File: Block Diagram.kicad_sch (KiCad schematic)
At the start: 0 parts

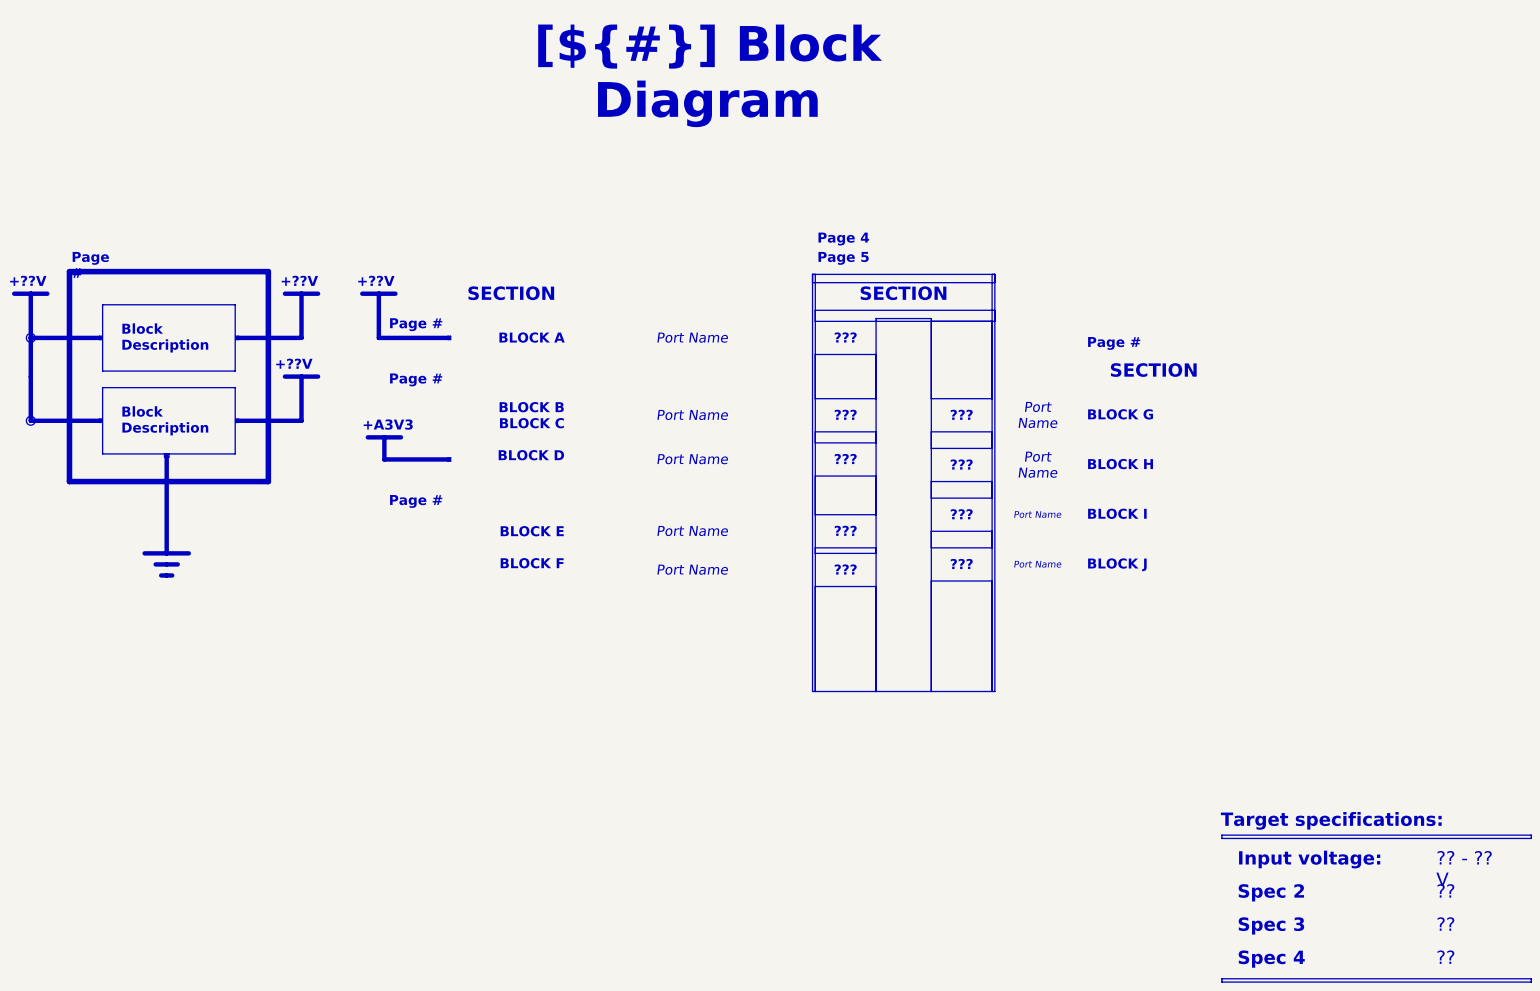
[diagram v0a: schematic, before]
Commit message: feat: Added some design notes, fixed some values in line with sim
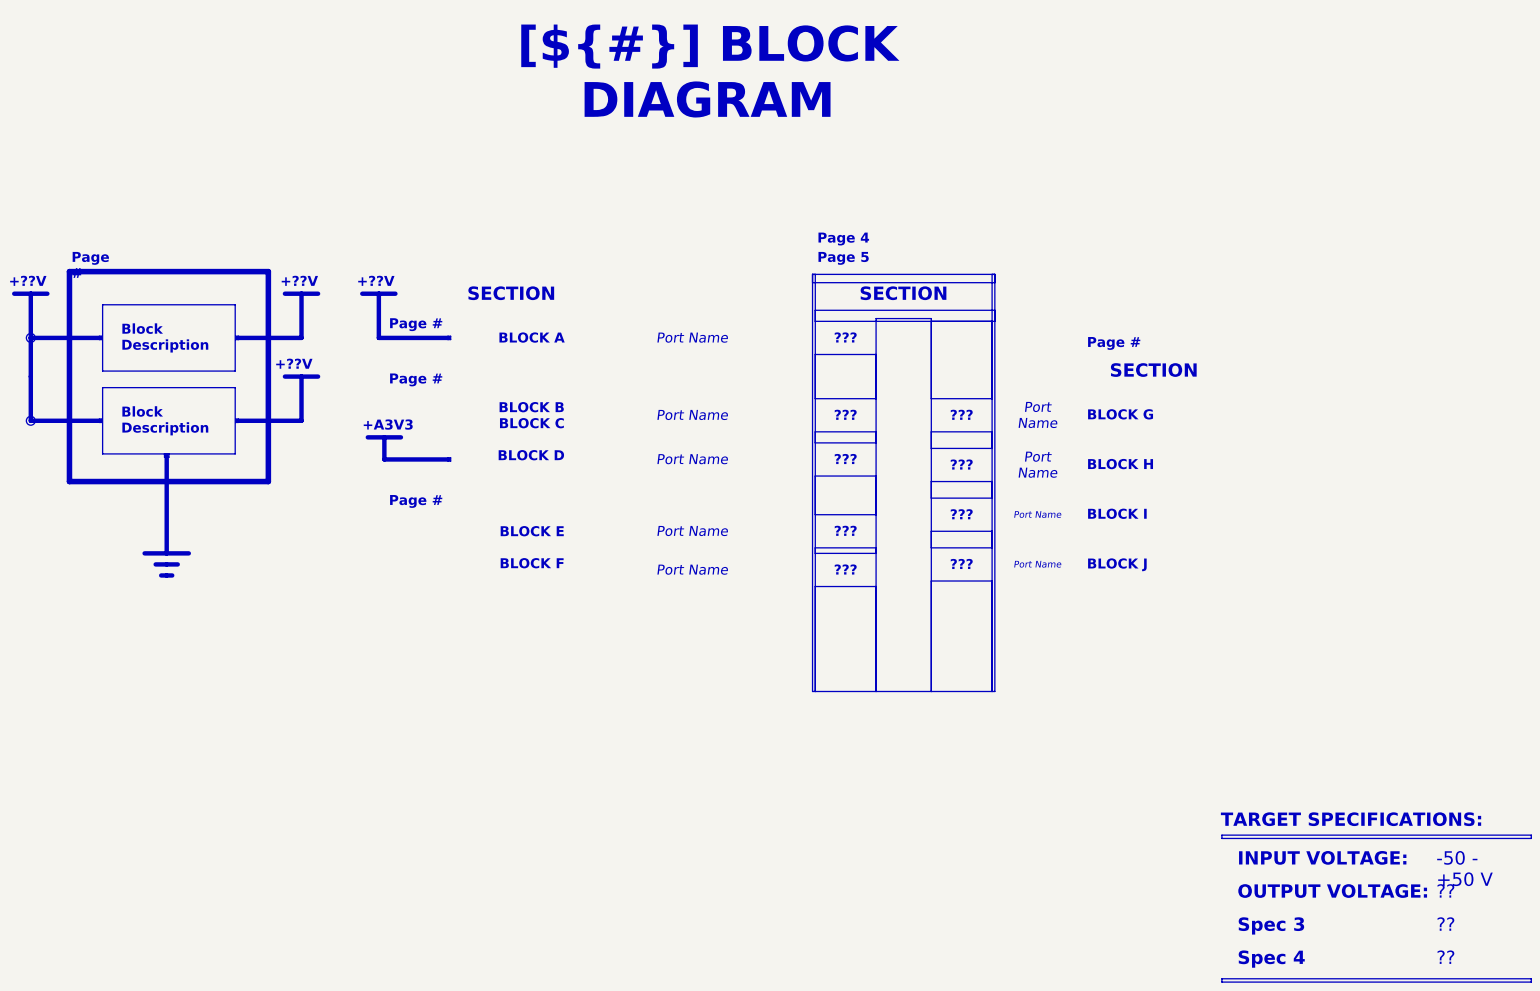
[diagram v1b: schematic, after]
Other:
- title: Block Diagram -> BLOCK DIAGRAM
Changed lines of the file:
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@@
 	(paper "A3")
 	(title_block
-		(title "Block Diagram")
+		(title "BLOCK DIAGRAM")
 		(date "2025-01-12")
 		(rev "${REVISION}")
@@
 		)
 	)
-	(text_box "?? - ?? V"
+	(text_box "-50 - +50 V"
 		(exclude_from_sim no)
 		(at 375.412 203.2 0)
-		(size 24.13 7.62)
+		(size 25.908 7.62)
 		(margins 2.2859 2.2859 2.2859 2.2859)
 		(stroke
 			(width -0.0001)
-			(type default)
+			(type solid)
 		)
 		(fill
@@
 		)
 	)
-	(text_box "Input voltage:"
+	(text_box "INPUT VOLTAGE:"
 		(exclude_from_sim no)
 		(at 329.692 203.2 0)
-		(size 41.91 7.62)
+		(size 47.498 7.62)
 		(margins 2.2859 2.2859 2.2859 2.2859)
 		(stroke
 			(width -0.0001)
-			(type default)
+			(type solid)
 		)
 		(fill
@@
 		)
 	)
-	(text_box "Target specifications:"
+	(text_box "TARGET SPECIFICATIONS:"
 		(exclude_from_sim no)
 		(at 325.882 194.31 0)
@@
 		(stroke
 			(width -0.0001)
-			(type default)
+			(type solid)
 		)
 		(fill
@@
 		)
 	)
-	(text_box "Spec 2"
+	(text_box "OUTPUT VOLTAGE:"
 		(exclude_from_sim no)
 		(at 329.692 210.82 0)
-		(size 43.18 7.62)
+		(size 46.228 7.62)
 		(margins 2.2859 2.2859 2.2859 2.2859)
 		(stroke
 			(width -0.0001)
-			(type default)
-		)
-		(fill
+			(type solid)
+		)
+		(fill
